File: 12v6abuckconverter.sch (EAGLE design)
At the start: 6 parts, among them J1 B06B-HCMKK

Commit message: Add files via upload
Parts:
- added D1: BYV95, diode:BYV95
- added U$3: BUCK1.6A, buck_1.6:BUCK1.6A
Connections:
- removed net JIMVOUT: C2.1, J1.4, U$1.S, U$1.VOUT
- new net LED: D1.C, J1.4
- new net N$1: C2.1, D1.A, U$1.S, U$1.VOUT
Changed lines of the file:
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@@
 <part name="U$2" library="REV BLDC" deviceset="SB50" device=""/>
 <part name="J1" library="B06B-HCMKK" deviceset="B06B-HCMKK" device=""/>
+<part name="D1" library="diode" library_urn="urn:adsk.eagle:library:210" deviceset="BYV95" device="" package3d_urn="urn:adsk.eagle:package:43367/1"/>
+<part name="U$3" library="buck_1.6" deviceset="BUCK1.6A" device=""/>
 </parts>
 <sheets>
@@
 <instance part="C1" gate="G$1" x="17.78" y="60.96" smashed="yes">
 <attribute name="NAME" x="18.796" y="61.595" size="1.778" layer="95"/>
-<attribute name="VALUE" x="18.796" y="56.769" size="1.778" layer="96"/>
+<attribute name="VALUE" x="13.716" y="56.769" size="1.778" layer="96"/>
 </instance>
 <instance part="C2" gate="G$1" x="55.88" y="53.34" smashed="yes">
@@
 <instance part="U$2" gate="G$1" x="-10.16" y="58.42" smashed="yes" rot="MR0"/>
 <instance part="J1" gate="G$1" x="71.12" y="55.88" smashed="yes">
-<attribute name="NAME" x="87.63" y="63.5" size="1.778" layer="95" align="center-left"/>
-<attribute name="VALUE" x="87.63" y="60.96" size="1.778" layer="96" align="center-left"/>
+<attribute name="NAME" x="67.31" y="55.88" size="1.778" layer="95" align="center-left"/>
+<attribute name="VALUE" x="59.69" y="58.42" size="1.778" layer="96" align="center-left"/>
 </instance>
+<instance part="D1" gate="1" x="63.5" y="63.5" smashed="yes"/>
+<instance part="U$3" gate="G$1" x="20.32" y="33.02" smashed="yes"/>
 </instances>
 <busses>
 </busses>
 <nets>
-<net name="JIMVOUT" class="0">
+<net name="LED" class="0">
 <segment>
-<pinref part="U$1" gate="G$1" pin="VOUT"/>
-<pinref part="U$1" gate="G$1" pin="S"/>
-<wire x1="45.72" y1="63.5" x2="45.72" y2="58.42" width="0.1524" layer="91"/>
-<wire x1="45.72" y1="63.5" x2="55.88" y2="63.5" width="0.1524" layer="91"/>
-<junction x="45.72" y="63.5"/>
-<pinref part="C2" gate="G$1" pin="1"/>
-<wire x1="55.88" y1="63.5" x2="55.88" y2="55.88" width="0.1524" layer="91"/>
-<wire x1="55.88" y1="63.5" x2="99.06" y2="63.5" width="0.1524" layer="91"/>
-<junction x="55.88" y="63.5"/>
 <pinref part="J1" gate="G$1" pin="4"/>
 <wire x1="99.06" y1="63.5" x2="99.06" y2="53.34" width="0.1524" layer="91"/>
 <wire x1="99.06" y1="53.34" x2="91.44" y2="53.34" width="0.1524" layer="91"/>
-<label x="104.14" y="66.04" size="1.778" layer="95"/>
+<wire x1="66.04" y1="63.5" x2="99.06" y2="63.5" width="0.1524" layer="91"/>
+<pinref part="D1" gate="1" pin="C"/>
+<label x="66.04" y="66.04" size="1.778" layer="95"/>
 </segment>
 </net>
@@
 <pinref part="J1" gate="G$1" pin="5"/>
 <wire x1="71.12" y1="43.18" x2="71.12" y2="50.8" width="0.1524" layer="91"/>
-<label x="78.74" y="40.64" size="1.778" layer="95"/>
+<label x="60.96" y="43.18" size="1.778" layer="95"/>
 </segment>
 </net>
@@
 <wire x1="91.44" y1="55.88" x2="104.14" y2="55.88" width="0.1524" layer="91"/>
 <wire x1="104.14" y1="55.88" x2="104.14" y2="27.94" width="0.1524" layer="91"/>
-<label x="114.3" y="58.42" size="1.778" layer="95"/>
+<label x="104.14" y="50.8" size="1.778" layer="95"/>
 </segment>
 </net>
@@
 </segment>
 </net>
+<net name="N$1" class="0">
+<segment>
+<pinref part="U$1" gate="G$1" pin="S"/>
+<pinref part="C2" gate="G$1" pin="1"/>
+<wire x1="55.88" y1="63.5" x2="55.88" y2="55.88" width="0.1524" layer="91"/>
+<junction x="55.88" y="63.5"/>
+<wire x1="55.88" y1="63.5" x2="60.96" y2="63.5" width="0.1524" layer="91"/>
+<pinref part="U$1" gate="G$1" pin="VOUT"/>
+<wire x1="45.72" y1="63.5" x2="55.88" y2="63.5" width="0.1524" layer="91"/>
+<junction x="45.72" y="63.5"/>
+<wire x1="45.72" y1="63.5" x2="45.72" y2="58.42" width="0.1524" layer="91"/>
+<pinref part="D1" gate="1" pin="A"/>
+</segment>
+</net>

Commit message: Add files via upload
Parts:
- C1, C2: device rcl:C-US025-024X044 -> rcl:C-USC0805
- F1: value 5A -> 7.5A
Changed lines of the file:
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@@
 <parts>
 <part name="U$1" library="12v6aBuckConverter" deviceset="12V6ABUCKCONVERTER" device=""/>
-<part name="F1" library="special" library_urn="urn:adsk.eagle:library:367" deviceset="FUSE" device="" package3d_urn="urn:adsk.eagle:package:26650/1" value="5A"/>
-<part name="C1" library="rcl" library_urn="urn:adsk.eagle:library:334" deviceset="C-US" device="025-024X044" package3d_urn="urn:adsk.eagle:package:23630/1" value="66uF"/>
-<part name="C2" library="rcl" library_urn="urn:adsk.eagle:library:334" deviceset="C-US" device="025-024X044" package3d_urn="urn:adsk.eagle:package:23630/1" value="10uF"/>
+<part name="F1" library="special" library_urn="urn:adsk.eagle:library:367" deviceset="FUSE" device="" package3d_urn="urn:adsk.eagle:package:26650/1" value="7.5A"/>
 <part name="U$2" library="REV BLDC" deviceset="SB50" device=""/>
 <part name="J1" library="B06B-HCMKK" deviceset="B06B-HCMKK" device=""/>
 <part name="D1" library="diode" library_urn="urn:adsk.eagle:library:210" deviceset="BYV95" device="" package3d_urn="urn:adsk.eagle:package:43367/1"/>
 <part name="U$3" library="buck_1.6" deviceset="BUCK1.6A" device=""/>
+<part name="C1" library="rcl" library_urn="urn:adsk.eagle:library:334" deviceset="C-US" device="C0805" package3d_urn="urn:adsk.eagle:package:23617/2" value="66uF"/>
+<part name="C2" library="rcl" library_urn="urn:adsk.eagle:library:334" deviceset="C-US" device="C0805" package3d_urn="urn:adsk.eagle:package:23617/2" value="10uF"/>
 </parts>
 <sheets>
@@
 <attribute name="VALUE" x="2.54" y="59.69" size="1.778" layer="96"/>
 </instance>
-<instance part="C1" gate="G$1" x="17.78" y="60.96" smashed="yes">
-<attribute name="NAME" x="18.796" y="61.595" size="1.778" layer="95"/>
-<attribute name="VALUE" x="13.716" y="56.769" size="1.778" layer="96"/>
-</instance>
-<instance part="C2" gate="G$1" x="55.88" y="53.34" smashed="yes">
-<attribute name="NAME" x="56.896" y="53.975" size="1.778" layer="95"/>
-<attribute name="VALUE" x="56.896" y="49.149" size="1.778" layer="96"/>
-</instance>
 <instance part="U$2" gate="G$1" x="-10.16" y="58.42" smashed="yes" rot="MR0"/>
 <instance part="J1" gate="G$1" x="71.12" y="55.88" smashed="yes">
@@
 <instance part="D1" gate="1" x="63.5" y="63.5" smashed="yes"/>
 <instance part="U$3" gate="G$1" x="20.32" y="33.02" smashed="yes"/>
+<instance part="C1" gate="G$1" x="17.78" y="60.96" smashed="yes">
+<attribute name="NAME" x="18.796" y="61.595" size="1.778" layer="95"/>
+<attribute name="VALUE" x="18.796" y="56.769" size="1.778" layer="96"/>
+</instance>
+<instance part="C2" gate="G$1" x="55.88" y="53.34" smashed="yes">
+<attribute name="NAME" x="56.896" y="53.975" size="1.778" layer="95"/>
+<attribute name="VALUE" x="56.896" y="49.149" size="1.778" layer="96"/>
+</instance>
 </instances>
 <busses>
@@
 <pinref part="U$1" gate="G$1" pin="-VOUT"/>
 <wire x1="45.72" y1="48.26" x2="45.72" y2="43.18" width="0.1524" layer="91"/>
+<junction x="45.72" y="43.18"/>
+<wire x1="45.72" y1="43.18" x2="55.88" y2="43.18" width="0.1524" layer="91"/>
+<pinref part="J1" gate="G$1" pin="5"/>
+<wire x1="55.88" y1="43.18" x2="71.12" y2="43.18" width="0.1524" layer="91"/>
+<wire x1="71.12" y1="43.18" x2="71.12" y2="50.8" width="0.1524" layer="91"/>
+<label x="60.96" y="43.18" size="1.778" layer="95"/>
 <pinref part="C2" gate="G$1" pin="2"/>
 <wire x1="55.88" y1="48.26" x2="55.88" y2="43.18" width="0.1524" layer="91"/>
-<wire x1="55.88" y1="43.18" x2="45.72" y2="43.18" width="0.1524" layer="91"/>
-<junction x="45.72" y="43.18"/>
-<wire x1="55.88" y1="43.18" x2="71.12" y2="43.18" width="0.1524" layer="91"/>
 <junction x="55.88" y="43.18"/>
-<pinref part="J1" gate="G$1" pin="5"/>
-<wire x1="71.12" y1="43.18" x2="71.12" y2="50.8" width="0.1524" layer="91"/>
-<label x="60.96" y="43.18" size="1.778" layer="95"/>
 </segment>
 </net>
@@
 <net name="N$4" class="0">
 <segment>
-<pinref part="C1" gate="G$1" pin="2"/>
 <wire x1="17.78" y1="55.88" x2="17.78" y2="53.34" width="0.1524" layer="91"/>
 <pinref part="U$1" gate="G$1" pin="-VIN"/>
@@
 <pinref part="U$2" gate="G$1" pin="-"/>
 <wire x1="-2.54" y1="55.88" x2="17.78" y2="55.88" width="0.1524" layer="91"/>
+<pinref part="C1" gate="G$1" pin="2"/>
 <junction x="17.78" y="55.88"/>
 </segment>
@@
 <segment>
 <pinref part="U$1" gate="G$1" pin="S"/>
-<pinref part="C2" gate="G$1" pin="1"/>
-<wire x1="55.88" y1="63.5" x2="55.88" y2="55.88" width="0.1524" layer="91"/>
-<junction x="55.88" y="63.5"/>
-<wire x1="55.88" y1="63.5" x2="60.96" y2="63.5" width="0.1524" layer="91"/>
 <pinref part="U$1" gate="G$1" pin="VOUT"/>
 <wire x1="45.72" y1="63.5" x2="55.88" y2="63.5" width="0.1524" layer="91"/>
 <junction x="45.72" y="63.5"/>
+<wire x1="55.88" y1="63.5" x2="60.96" y2="63.5" width="0.1524" layer="91"/>
 <wire x1="45.72" y1="63.5" x2="45.72" y2="58.42" width="0.1524" layer="91"/>
 <pinref part="D1" gate="1" pin="A"/>
+<pinref part="C2" gate="G$1" pin="1"/>
+<wire x1="55.88" y1="55.88" x2="55.88" y2="63.5" width="0.1524" layer="91"/>
+<junction x="55.88" y="63.5"/>
 </segment>
 </net>

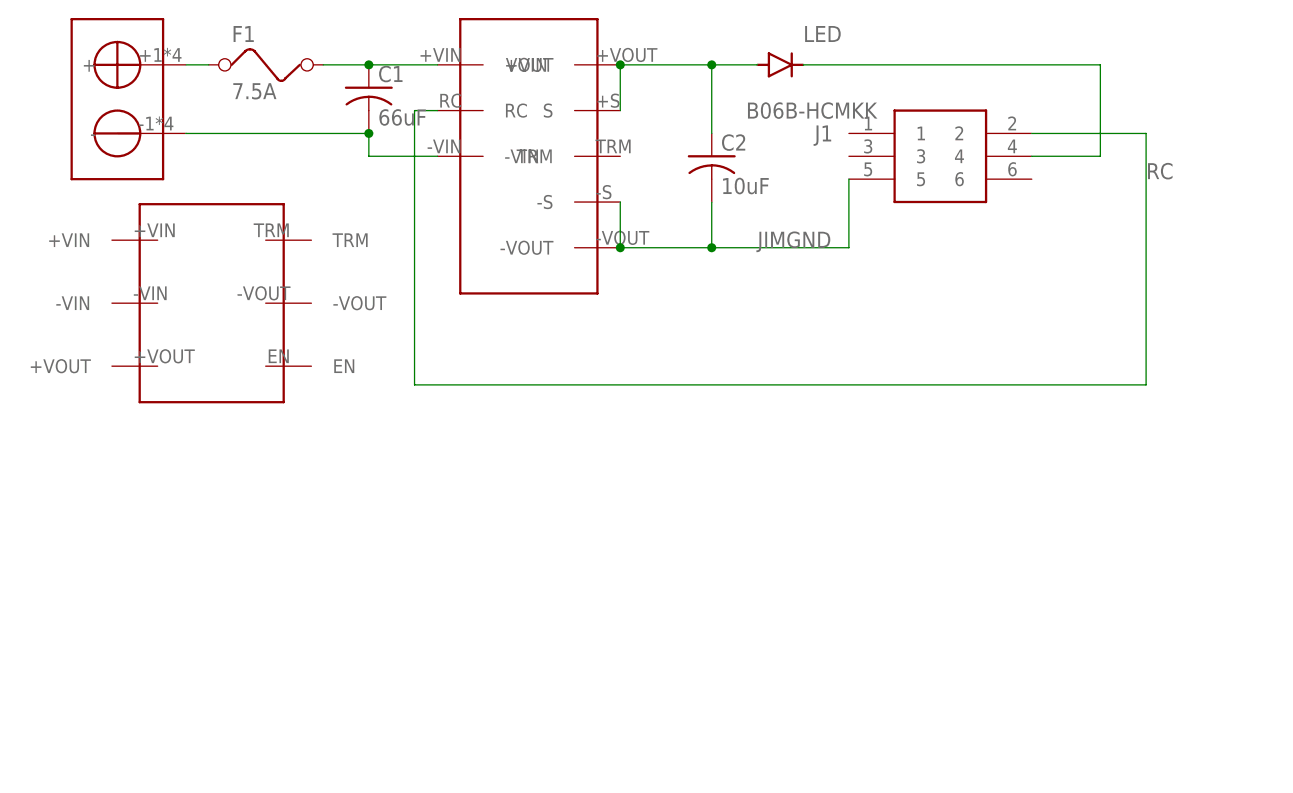
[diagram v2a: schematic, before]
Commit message: Update the schematic with new buckboard
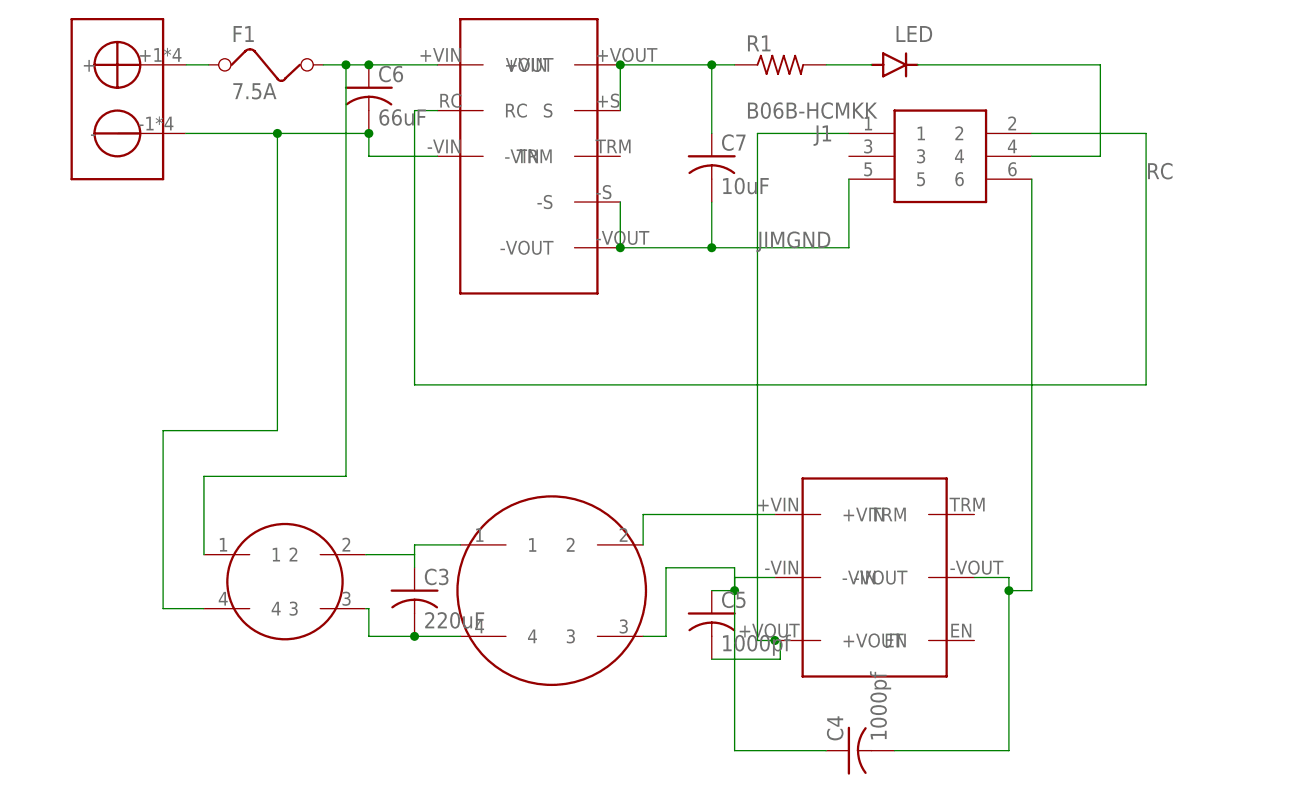
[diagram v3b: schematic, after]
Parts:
- added BUCK150UH: CMNMODECHOKE150UH, cmnModeChoke150uH:CMNMODECHOKE150UH
- added C3: 220uF, rcl:C-USC0805
- added C4, C5: 1000pf, rcl:C-USC0805
- added R1: (no value), rcl:R-US_R0805
- added U$4: CMNMODECHOKE1.2MH, cmnModeChoke1.2mH:CMNMODECHOKE1.2MH
- renumbered C1 to C6, C2 to C7
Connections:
- new net N$10: U$3.+VIN, U$4.2
- new net N$11: BUCK150UH.4, C6.2, U$1.-VIN, U$2.-
- new net N$2: BUCK150UH.2, C3.1, U$4.1
- new net N$5: BUCK150UH.3, C3.2, U$4.4
- new net N$7: C4.1, C5.1, U$3.-VIN, U$4.3
- new net N$8: C4.2, J1.6, U$3.-VOUT
- new net N$9: C5.2, J1.1, U$3.+VOUT
- net N$1: now also R1.1; no longer D1.A
- net N$3: now also BUCK150UH.1
- net N$4: now also D1.A, R1.2; no longer C6.2, U$1.-VIN, U$2.-
